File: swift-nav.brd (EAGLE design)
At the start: 53 x 53 mm, 169 parts, among them J1 SMA_EDGE, J6 ZX62-B-5PA, U1 6SLX9FTG256, U10 MAX2769, U12 PT7M8206B33TA5EX, U13 M25PX80, U2 LTC3407A_DFN, U3 STM32-M-64-LQFP, U4 7Q-16.368MBG-T, U5 SMA_PATCH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

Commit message: Looots of stuff
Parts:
- removed U$1: LOGO, swift-nav:LOGO1
- added C95: 100pF, rcl:C0402
- added Q1: MOSFET-PCHANNELSMD, SparkFun-DiscreteSemi:SOT23-3
- C15, C16: device rcl:C0603K -> rcl:C0402
- moved C70 2.31 mm to (24.6, 16.5), turned to 90 degrees
- moved R62 1.41 mm to (20.2, 12.1)
- moved C1 1.37 mm to (18.9, 12.7)
- moved R61 1.35 mm to (17.8, 12.7)
- moved R28 1.09 mm to (16.8, 12.4)
- moved C15 1.01 mm to (37.3, 26.6), turned to 90 degrees
- moved U2 0.74 mm to (27.1, 15.6)
- moved R30 0.63 mm to (16.0, 12.4)
- moved D1 0.61 mm to (30.3, 16.0), turned to 90 degrees
- moved C16 0.59 mm to (35.6, 27.7)
- moved R8 0.57 mm to (19.9, 14.6)
- moved L13 0.19 mm to (28.5, 12.0)
- moved C2 0.08 mm to (24.4, 11.9)
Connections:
- new net N$18: C2.1, Q1.2, R1.2, U2.2, U2.3, U2.6, U2.9
- new net N$35: C15.2, C16.1, C95.1
- net GND: now also Q1.1
- net N$11: now also C95.2; no longer C15.2, C16.1
- net UART1_RX: now also X6.2; no longer X6.5
- net UART1_TX: now also X6.3; no longer X6.4
- net UART3_RX: now also X1.2; no longer X1.5
- net UART3_TX: now also X1.3; no longer X1.4
- net V+: now also Q1.3, X1.5, X6.5; no longer C2.1, R1.2, U2.2, U2.3, U2.6, U2.9, X1.2, X6.2
- net VCCIO: now also X1.4, X6.4; no longer X1.3, X6.3
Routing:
- net N$18: track 0.00 -> 20.4 mm, vias 0 -> 3
- net GND: track 97.8 -> 91.5 mm, vias 405 -> 404
- net UART3_RX: track 26.9 -> 22.2 mm
- net UART1_RX: track 19.3 -> 15.2 mm
- net N$53: track 6.71 -> 10.1 mm
- net V+: track 134.1 -> 137.3 mm, vias 13 -> 12
- net N$11: track 5.02 -> 1.89 mm
- net N$35: track 0.00 -> 2.65 mm
- net VCCIO: track 164.8 -> 167.1 mm
- net V_USB: track 115.0 -> 117.0 mm, vias 6 -> 8
- net N$55: track 23.9 -> 25.5 mm
- net UART3_TX: track 25.3 -> 23.8 mm
- net N$24: track 19.4 -> 20.6 mm
- net FTDI_NRST: track 110.2 -> 109.5 mm
- net UART6_TX: track 52.1 -> 51.3 mm
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
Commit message: More stuff
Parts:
- added L3: 250nH/DNP, pel_dipol_comp:0402-IND
- L1: value 250nH/DNP -> 250nH
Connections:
- net N$10: now also L3.P$1
- net N$14: now also L3.P$2
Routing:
- net N$10: track 16.0 -> 32.9 mm, vias 2 -> 3
- net N$14: track 1.72 -> 2.30 mm

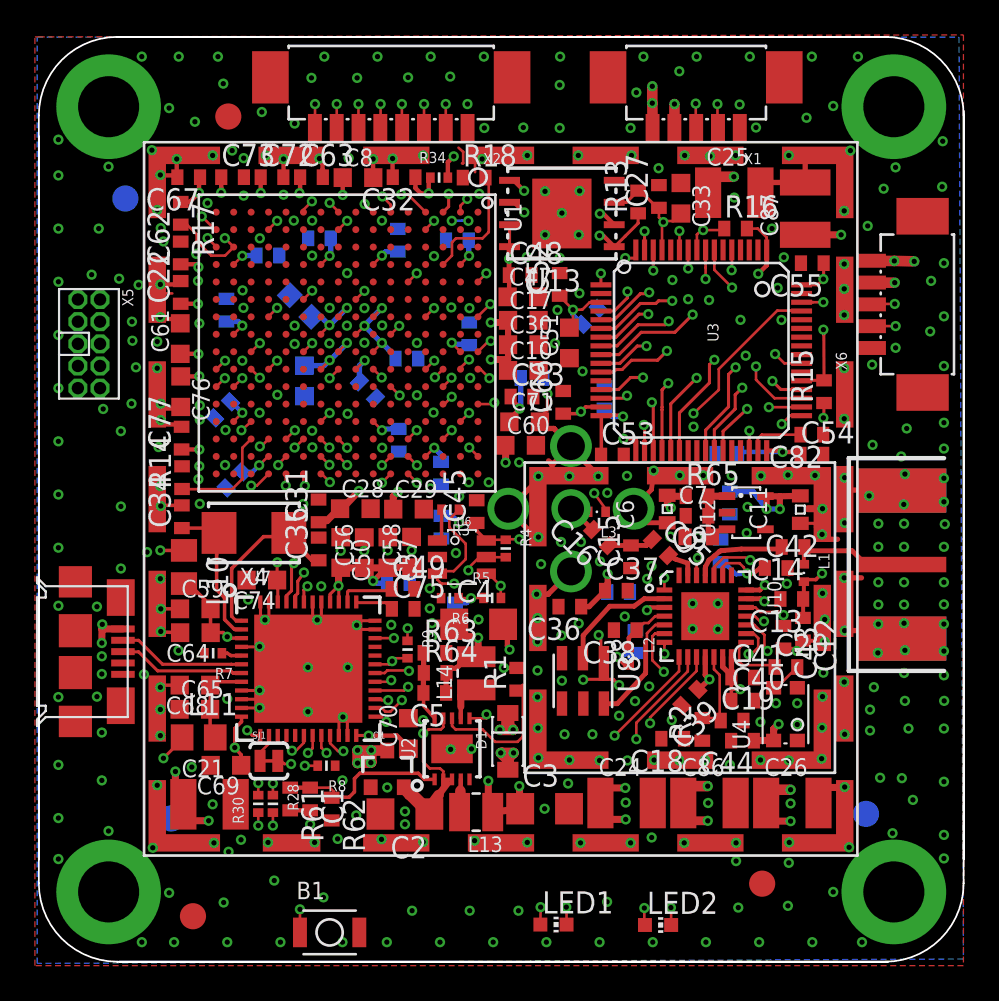
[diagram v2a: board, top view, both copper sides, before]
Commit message: Changed FT232 AC7 pullup to V_USB instead of VCCIO Changed RF input from V+ (before PMOS) to VDD (after PMOS) Added pulldown resistor to V_USB
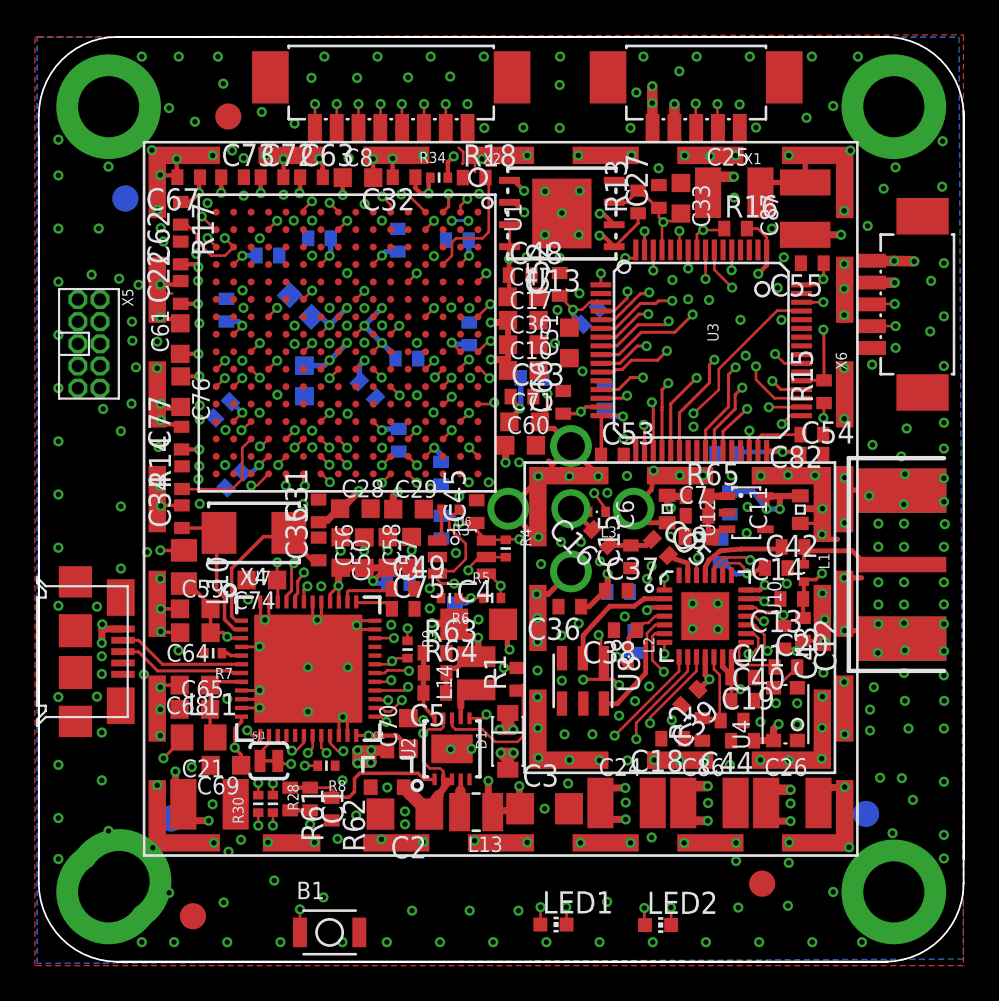
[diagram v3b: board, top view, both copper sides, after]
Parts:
- added H5: MOUNT-PAD-ROUNDM3, swift-nav:M3-PAD
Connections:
- removed net N$18: C2.1, Q1.2, R1.2, U2.2, U2.3, U2.6, U2.9
- new net VDD: C2.1, C6.2, Q1.2, R1.2, R65.1, U2.2, U2.3, U2.6, U2.9
- net V+: no longer C6.2, R65.1
- net VCCIO: no longer R9.P$1
- net V_USB: now also R9.P$1
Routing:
- net VDD: track 0.00 -> 21.5 mm, vias 0 -> 3
- net N$18: track 20.4 -> 0.00 mm, vias 3 -> 0
- net V+: track 137.3 -> 135.7 mm
- net VCCIO: track 167.1 -> 166.1 mm, vias 76 -> 75
- net V_USB: track 117.0 -> 118.1 mm, vias 8 -> 9
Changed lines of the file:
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@@
 <setting verticaltext="up"/>
 </settings>
-<grid distance="1" unitdist="mil" unit="mil" style="lines" multiple="1" display="yes" altdistance="0.01" altunitdist="mm" altunit="mm"/>
+<grid distance="0.1" unitdist="mm" unit="mm" style="lines" multiple="1" display="yes" altdistance="0.01" altunitdist="mm" altunit="mm"/>
 <layers>
 <layer number="1" name="Top" color="4" fill="1" visible="yes" active="yes"/>
@@
 <element name="C95" library="rcl" package="C0402" value="100pF" x="39.0218375" y="27.138996875" rot="R315"/>
 <element name="L3" library="pel_dipol_comp" package="0402-IND" value="250nH/DNP" x="35.3822" y="29.1846" rot="R180"/>
+<element name="H5" library="swift-nav" package="M3-PAD" value="MOUNT-PAD-ROUNDM3" x="8" y="8"/>
 </elements>
 <signals>
@@
 <contactref element="R6" pad="P$1"/>
 <contactref element="C45" pad="1"/>
-<contactref element="R9" pad="P$1"/>
 <contactref element="U7" pad="40"/>
 <contactref element="U7" pad="39"/>
@@
 <via x="12.5984" y="32.7533" extent="1-16" drill="0.3"/>
 <wire x1="12.5984" y1="32.7533" x2="12.5984" y2="32.8168" width="0.254" layer="3"/>
-<wire x1="24.529" y1="21.7906" x2="24.529" y2="22.497" width="0.1524" layer="1"/>
-<wire x1="24.529" y1="22.497" x2="24.5364" y2="22.5044" width="0.1524" layer="1"/>
-<via x="24.5364" y="22.5044" extent="1-16" drill="0.3"/>
-<wire x1="24.5364" y1="22.5044" x2="24.5364" y2="22.5298" width="0.1524" layer="3"/>
 <wire x1="15.9766" y1="12.946" x2="15.9766" y2="13.6398" width="0.1524" layer="1"/>
 <via x="15.9766" y="13.6398" extent="1-16" drill="0.3"/>
@@
 <wire x1="30.1498" y1="32.9832" x2="30.1498" y2="32.004" width="0.4064" layer="1"/>
 <via x="30.1498" y="32.004" extent="1-16" drill="0.3"/>
-<wire x1="24.5364" y1="22.5298" x2="24.3586" y2="22.352" width="0.4064" layer="3"/>
-<wire x1="24.3586" y1="22.352" x2="24.3586" y2="22.3012" width="0.4064" layer="3"/>
 <wire x1="11.6826" y1="12.4206" x2="11.6572" y2="13.2094" width="0.4064" layer="1"/>
 <wire x1="11.6572" y1="13.2094" x2="11.2268" y2="13.6398" width="0.4064" layer="1"/>
@@
 </signal>
 <signal name="V+">
-<contactref element="C6" pad="2"/>
-<contactref element="R65" pad="1"/>
 <contactref element="D1" pad="2"/>
-<wire x1="39.410809375" y1="30.131090625" x2="39.4208" y2="29.6164" width="0.4064" layer="1"/>
 <wire x1="39.4208" y1="29.6164" x2="39.61891875" y2="29.41528125" width="0.4064" layer="1"/>
 <via x="39.61891875" y="29.41528125" extent="1-16" drill="0.3"/>
-<wire x1="39.410809375" y1="30.131090625" x2="39.4937" y2="30.0736" width="0.4064" layer="1"/>
-<wire x1="39.4937" y1="30.0736" x2="40.4726" y2="30.0736" width="0.4064" layer="1"/>
 <via x="30.5816" y="16.6878" extent="1-16" drill="0.3"/>
 <via x="29.8196" y="16.6878" extent="1-16" drill="0.3"/>
@@
 <wire x1="24.4094" y1="11.303" x2="24.384" y2="11.2776" width="0.6096" layer="2"/>
 <wire x1="23.9268" y1="12.4714" x2="24.384" y2="12.0142" width="0.4064" layer="15"/>
+<contactref element="R9" pad="P$1"/>
+<wire x1="24.529" y1="21.7906" x2="24.529" y2="22.497" width="0.1524" layer="1"/>
+<wire x1="24.529" y1="22.497" x2="24.5364" y2="22.5044" width="0.1524" layer="1"/>
+<via x="24.5364" y="22.5044" extent="1-16" drill="0.3"/>
+<wire x1="24.5364" y1="22.5044" x2="24.5364" y2="22.5298" width="0.1524" layer="3"/>
+<wire x1="24.5364" y1="22.5298" x2="24.3586" y2="22.352" width="0.4064" layer="3"/>
+<wire x1="24.3586" y1="22.352" x2="24.3586" y2="22.3012" width="0.4064" layer="3"/>
+<wire x1="29.21" y1="15.367" x2="24.529" y2="21.7906" width="0" layer="19" extent="1-2"/>
 </signal>
 <signal name="FTDI_ADBUS5">
@@
 <wire x1="16.1036" y1="14.9352" x2="16.0782" y2="14.9098" width="0.1524" layer="1"/>
 </signal>
-<signal name="N$18">
+<signal name="N$35">
+<contactref element="C15" pad="2"/>
+<contactref element="C16" pad="1"/>
+<wire x1="37.336190625" y1="27.256871875" x2="36.05448125" y2="27.249225" width="0.2794" layer="1"/>
+<contactref element="C95" pad="1"/>
+<wire x1="38.562215625" y1="27.598615625" x2="38.220471875" y2="27.256871875" width="0.2794" layer="1"/>
+<wire x1="38.220471875" y1="27.256871875" x2="37.336190625" y2="27.256871875" width="0.2794" layer="1"/>
+</signal>
+<signal name="VDD">
 <contactref element="U2" pad="6"/>
 <contactref element="U2" pad="3"/>
@@
 <contactref element="U2" pad="2"/>
 <contactref element="C2" pad="1"/>
+<contactref element="Q1" pad="2"/>
 <wire x1="26.580509375" y1="17.3498" x2="26.580509375" y2="16.852309375" width="0.1524" layer="1"/>
 <wire x1="26.580509375" y1="16.852309375" x2="26.4414" y2="16.7132" width="0.1524" layer="1"/>
@@
 <wire x1="27.9384" y1="17.9816" x2="30.0482" y2="20.2438" width="0.1524" layer="2"/>
 <wire x1="26.580509375" y1="13.8498" x2="27.080509375" y2="13.8498" width="0.2032" layer="1"/>
-<contactref element="Q1" pad="2"/>
 <wire x1="26.580509375" y1="13.8498" x2="26.580509375" y2="13.321709375" width="0.254" layer="1"/>
 <wire x1="26.580509375" y1="13.321709375" x2="26.797" y2="13.6144" width="0.254" layer="1"/>
@@
 <wire x1="24.6888" y1="13.0302" x2="25.7796" y2="11.9394" width="0.762" layer="1"/>
 <wire x1="25.7796" y1="11.9394" x2="25.7796" y2="11.8646" width="1.4224" layer="1"/>
-</signal>
-<signal name="N$35">
-<contactref element="C15" pad="2"/>
-<contactref element="C16" pad="1"/>
-<wire x1="37.336190625" y1="27.256871875" x2="36.05448125" y2="27.249225" width="0.2794" layer="1"/>
-<contactref element="C95" pad="1"/>
-<wire x1="38.562215625" y1="27.598615625" x2="38.220471875" y2="27.256871875" width="0.2794" layer="1"/>
-<wire x1="38.220471875" y1="27.256871875" x2="37.336190625" y2="27.256871875" width="0.2794" layer="1"/>
+<contactref element="C6" pad="2"/>
+<contactref element="R65" pad="1"/>
+<wire x1="39.410809375" y1="30.131090625" x2="39.4937" y2="30.0736" width="0.4064" layer="1"/>
+<wire x1="39.4937" y1="30.0736" x2="40.4726" y2="30.0736" width="0.4064" layer="1"/>
+<wire x1="30.8132" y1="20.2364" x2="39.410809375" y2="30.131090625" width="0" layer="19" extent="1-1"/>
 </signal>
 </signals>

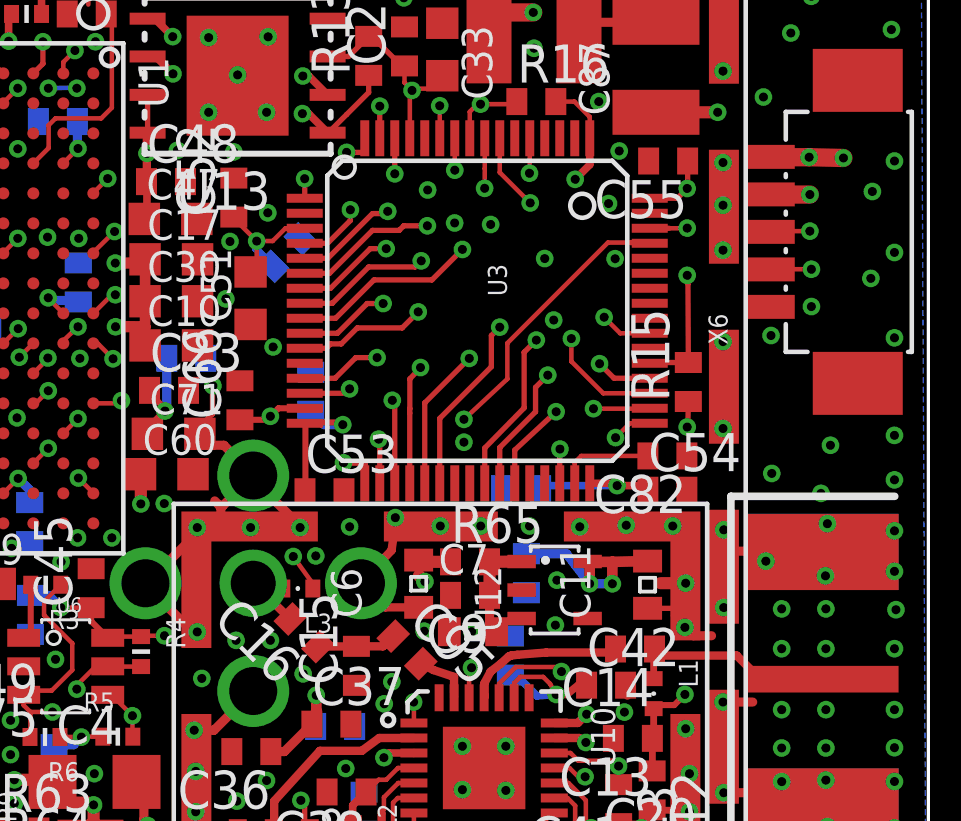
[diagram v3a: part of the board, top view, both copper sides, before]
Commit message: Changed FT232 AC7 pullup to V_USB instead of VCCIO Changed RF input from V+ (before PMOS) to VDD (after PMOS) Added pulldown resistor to V_USB
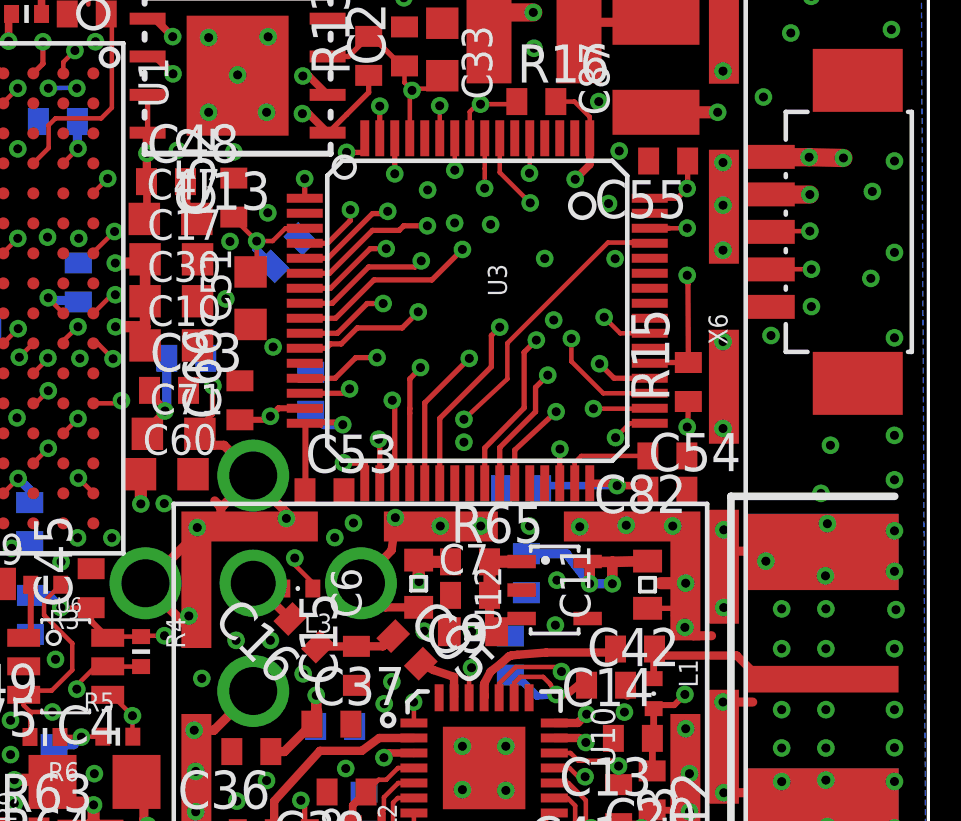
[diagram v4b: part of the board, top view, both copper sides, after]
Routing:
- net VDD: track 21.5 -> 44.6 mm, vias 3 -> 4
- net V+: track 135.7 -> 120.8 mm, vias 12 -> 10
- net V_USB: track 118.1 -> 133.0 mm
- net GND: track 91.5 -> 92.9 mm, vias 404 -> 403

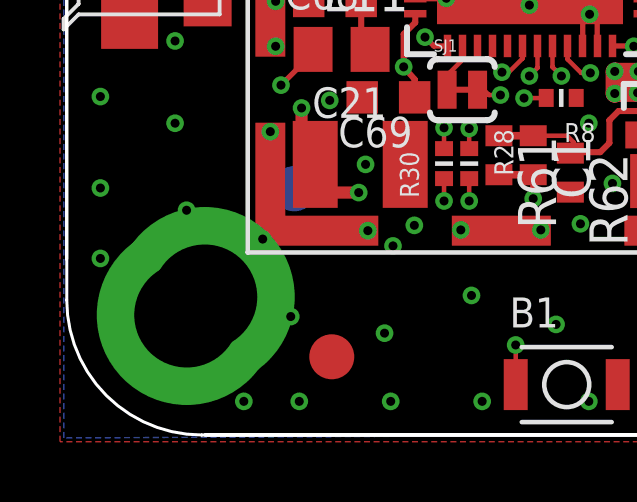
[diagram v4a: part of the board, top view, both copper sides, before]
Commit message: Removed extra mounting hole. Still need to move mounting holes in
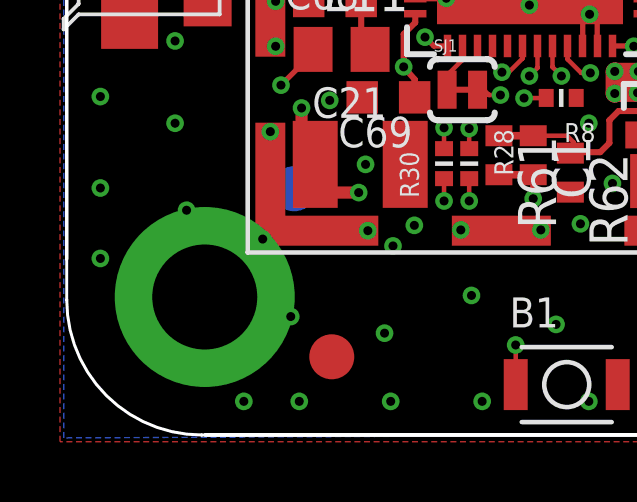
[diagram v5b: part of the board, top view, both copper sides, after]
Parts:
- removed H1: MOUNT-PAD-ROUNDM3, swift-nav:M3-PAD
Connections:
- net GND: now also H5.B3,0; no longer H1.B3,0
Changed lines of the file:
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@@
 <grid distance="1" unitdist="mil" unit="mil" style="lines" multiple="1" display="yes" altdistance="0.01" altunitdist="mm" altunit="mm"/>
 <layers>
-<layer number="1" name="Top" color="4" fill="1" visible="no" active="yes"/>
-<layer number="2" name="Route2" color="1" fill="3" visible="yes" active="yes"/>
+<layer number="1" name="Top" color="4" fill="1" visible="yes" active="yes"/>
+<layer number="2" name="Route2" color="1" fill="3" visible="no" active="yes"/>
 <layer number="3" name="Route3" color="4" fill="3" visible="no" active="yes"/>
 <layer number="4" name="Route4" color="1" fill="4" visible="no" active="no"/>
@@
 <layer number="112" name="2Restrict" color="7" fill="1" visible="no" active="yes"/>
 <layer number="116" name="Patch_BOT" color="9" fill="4" visible="no" active="yes"/>
-<layer number="121" name="_tplace" color="14" fill="1" visible="no" active="yes"/>
+<layer number="121" name="_tplace" color="14" fill="1" visible="yes" active="yes"/>
 <layer number="122" name="_bplace" color="14" fill="1" visible="no" active="yes"/>
 <layer number="123" name="tTestmark" color="7" fill="1" visible="no" active="yes"/>
@@
 <element name="X2" library="pel_molex" package="PB-53261-08" value="" x="23.5966" y="52.2832" rot="R180"/>
 <element name="C74" library="rcl" package="C0603K" value="0.047uF" x="16.1798" y="25.273" rot="R180"/>
-<element name="H1" library="swift-nav" package="M3-PAD" value="MOUNT-PAD-ROUNDM3" x="7.4" y="7.4"/>
 <element name="H2" library="swift-nav" package="M3-PAD" value="MOUNT-PAD-ROUNDM3" x="52.4" y="7.4"/>
 <element name="H3" library="swift-nav" package="M3-PAD" value="MOUNT-PAD-ROUNDM3" x="7.4" y="52.4"/>
@@
 <via x="52.9844" y="23.868" extent="1-16" drill="0.3"/>
 <via x="51.5112" y="23.868" extent="1-16" drill="0.3"/>
-<contactref element="H1" pad="B3,0"/>
 <contactref element="H2" pad="B3,0"/>
 <contactref element="H4" pad="B3,0"/>
@@
 <wire x1="32.0154" y1="41.6846" x2="31.7" y2="42" width="0.2032" layer="1"/>
 <wire x1="31.7" y1="42" x2="31.7" y2="42.7" width="0.2032" layer="1"/>
+<contactref element="H5" pad="B3,0"/>
+<wire x1="9.9314" y1="9.9314" x2="8" y2="8" width="0" layer="19" extent="1-1"/>
 </signal>
 <signal name="N$3">
